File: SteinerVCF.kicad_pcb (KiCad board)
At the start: 2 copper layers, 39.6 x 100 mm, 72 parts, among them J1 AudioJack2_Ground_Switch, J2 AudioJack2_Ground_Switch, J3 AudioJack2_Ground_Switch, J4 AudioJack2_Ground_Switch, J5 AudioJack2_Ground_Switch, J6 AudioJack2_Ground_Switch, J7 Conn_02x05_Odd_Even, J8 AudioJack2_Ground_Switch, J9 AudioJack2_Ground_Switch, Q1 BC847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

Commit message: Added bourns trimmer 3-d model.
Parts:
- RV4: footprint Potentiometer_THT:Potentiometer_Bourns_3296W_Vertical -> Local:Bourns3296WV
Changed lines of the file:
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@@
-(kicad_pcb (version 20171130) (host pcbnew "(5.0.1-3-g963ef8bb5)")
+(kicad_pcb (version 20171130) (host pcbnew "(5.0.0)")
   (general
     (thickness 1.6)
@@
     (aux_axis_origin 148.5 105)
     (grid_origin 148.5 105)
-    (visible_elements FFFFFF7F)
+    (visible_elements 7FFFFFFF)
     (pcbplotparams
       (layerselection 0x010f4_ffffffff)
@@
     (add_net "Net-(R9-Pad2)")
   )
+  (module Local:Bourns3296WV (layer B.Cu)
+    (at 164.883 102.46 90)
+    (descr "Potentiometer, vertical, Bourns 3296W, https://www.bourns.com/pdfs/3296.pdf")
+    (tags "Potentiometer vertical Bourns 3296W")
+    (fp_text reference RV4 (at -2.54 -3.429 90) (layer B.SilkS)
+      (effects (font (size 0.75 1) (thickness 0.125)) (justify mirror))
+    )
+    (fp_text value 2k (at -2.54 -3.67 90) (layer B.Fab)
+      (effects (font (size 1 1) (thickness 0.15)) (justify mirror))
+    )
+    (fp_circle (center 0.955 -1.15) (end 2.05 -1.15) (layer B.Fab) (width 0.1))
+    (fp_line (start -7.305 2.41) (end -7.305 -2.42) (layer B.Fab) (width 0.1))
+    (fp_line (start -7.305 -2.42) (end 2.225 -2.42) (layer B.Fab) (width 0.1))
+    (fp_line (start 2.225 -2.42) (end 2.225 2.41) (layer B.Fab) (width 0.1))
+    (fp_line (start 2.225 2.41) (end -7.305 2.41) (layer B.Fab) (width 0.1))
+    (fp_line (start 0.955 -2.235) (end 0.956 -0.066) (layer B.Fab) (width 0.1))
+    (fp_line (start 0.955 -2.235) (end 0.956 -0.066) (layer B.Fab) (width 0.1))
+    (fp_line (start -7.425 2.53) (end 2.345 2.53) (layer B.SilkS) (width 0.12))
+    (fp_line (start -7.425 -2.54) (end 2.345 -2.54) (layer B.SilkS) (width 0.12))
+    (fp_line (start -7.425 2.53) (end -7.425 -2.54) (layer B.SilkS) (width 0.12))
+    (fp_line (start 2.345 2.53) (end 2.345 -2.54) (layer B.SilkS) (width 0.12))
+    (fp_line (start -7.6 2.7) (end -7.6 -2.7) (layer B.CrtYd) (width 0.05))
+    (fp_line (start -7.6 -2.7) (end 2.5 -2.7) (layer B.CrtYd) (width 0.05))
+    (fp_line (start 2.5 -2.7) (end 2.5 2.7) (layer B.CrtYd) (width 0.05))
+    (fp_line (start 2.5 2.7) (end -7.6 2.7) (layer B.CrtYd) (width 0.05))
+    (fp_text user %R (at -3.175 -0.005 90) (layer B.Fab)
+      (effects (font (size 1 1) (thickness 0.15)) (justify mirror))
+    )
+    (pad 1 thru_hole circle (at 0 0 90) (size 1.44 1.44) (drill 0.8) (layers *.Cu *.Mask)
+      (net 27 "Net-(R9-Pad2)"))
+    (pad 2 thru_hole circle (at -2.54 0 90) (size 1.44 1.44) (drill 0.8) (layers *.Cu *.Mask)
+      (net 27 "Net-(R9-Pad2)"))
+    (pad 3 thru_hole circle (at -5.08 0 90) (size 1.44 1.44) (drill 0.8) (layers *.Cu *.Mask)
+      (net 55 GND))
+    (model ${KISYS3DMOD}/Potentiometer_THT.3dshapes/Potentiometer_Bourns_3296W_Vertical.wrl
+      (at (xyz 0 0 0))
+      (scale (xyz 1 1 1))
+      (rotate (xyz 0 0 0))
+    )
+    (model ${KIPRJMOD}/Local.pretty/Bourns3296WV.step
+      (offset (xyz -5 0 0))
+      (scale (xyz 1 1 1))
+      (rotate (xyz 90 0 0))
+    )
+  )
   (module Local:PJ398SM (layer F.Cu)
     (at 158.66 135.48)
@@
       (at (xyz 0 0 0))
       (scale (xyz 1 1 1))
-      (rotate (xyz 0 0 0))
-    )
-  )
-  (module Potentiometer_THT:Potentiometer_Bourns_3296W_Vertical (layer B.Cu)
-    (at 164.883 102.46 90)
-    (descr "Potentiometer, vertical, Bourns 3296W, https://www.bourns.com/pdfs/3296.pdf")
-    (tags "Potentiometer vertical Bourns 3296W")
-    (fp_text reference RV4 (at -2.54 -3.429 90) (layer B.SilkS)
-      (effects (font (size 0.75 1) (thickness 0.125)) (justify mirror))
-    )
-    (fp_text value 2k (at -2.54 -3.67 90) (layer B.Fab)
-      (effects (font (size 1 1) (thickness 0.15)) (justify mirror))
-    )
-    (fp_circle (center 0.955 -1.15) (end 2.05 -1.15) (layer B.Fab) (width 0.1))
-    (fp_line (start -7.305 2.41) (end -7.305 -2.42) (layer B.Fab) (width 0.1))
-    (fp_line (start -7.305 -2.42) (end 2.225 -2.42) (layer B.Fab) (width 0.1))
-    (fp_line (start 2.225 -2.42) (end 2.225 2.41) (layer B.Fab) (width 0.1))
-    (fp_line (start 2.225 2.41) (end -7.305 2.41) (layer B.Fab) (width 0.1))
-    (fp_line (start 0.955 -2.235) (end 0.956 -0.066) (layer B.Fab) (width 0.1))
-    (fp_line (start 0.955 -2.235) (end 0.956 -0.066) (layer B.Fab) (width 0.1))
-    (fp_line (start -7.425 2.53) (end 2.345 2.53) (layer B.SilkS) (width 0.12))
-    (fp_line (start -7.425 -2.54) (end 2.345 -2.54) (layer B.SilkS) (width 0.12))
-    (fp_line (start -7.425 2.53) (end -7.425 -2.54) (layer B.SilkS) (width 0.12))
-    (fp_line (start 2.345 2.53) (end 2.345 -2.54) (layer B.SilkS) (width 0.12))
-    (fp_line (start -7.6 2.7) (end -7.6 -2.7) (layer B.CrtYd) (width 0.05))
-    (fp_line (start -7.6 -2.7) (end 2.5 -2.7) (layer B.CrtYd) (width 0.05))
-    (fp_line (start 2.5 -2.7) (end 2.5 2.7) (layer B.CrtYd) (width 0.05))
-    (fp_line (start 2.5 2.7) (end -7.6 2.7) (layer B.CrtYd) (width 0.05))
-    (fp_text user %R (at -3.175 -0.005 90) (layer B.Fab)
-      (effects (font (size 1 1) (thickness 0.15)) (justify mirror))
-    )
-    (pad 1 thru_hole circle (at 0 0 90) (size 1.44 1.44) (drill 0.8) (layers *.Cu *.Mask)
-      (net 27 "Net-(R9-Pad2)"))
-    (pad 2 thru_hole circle (at -2.54 0 90) (size 1.44 1.44) (drill 0.8) (layers *.Cu *.Mask)
-      (net 27 "Net-(R9-Pad2)"))
-    (pad 3 thru_hole circle (at -5.08 0 90) (size 1.44 1.44) (drill 0.8) (layers *.Cu *.Mask)
-      (net 55 GND))
-    (model ${KISYS3DMOD}/Potentiometer_THT.3dshapes/Potentiometer_Bourns_3296W_Vertical.wrl
-      (at (xyz 0 0 0))
-      (scale (xyz 1 1 1))

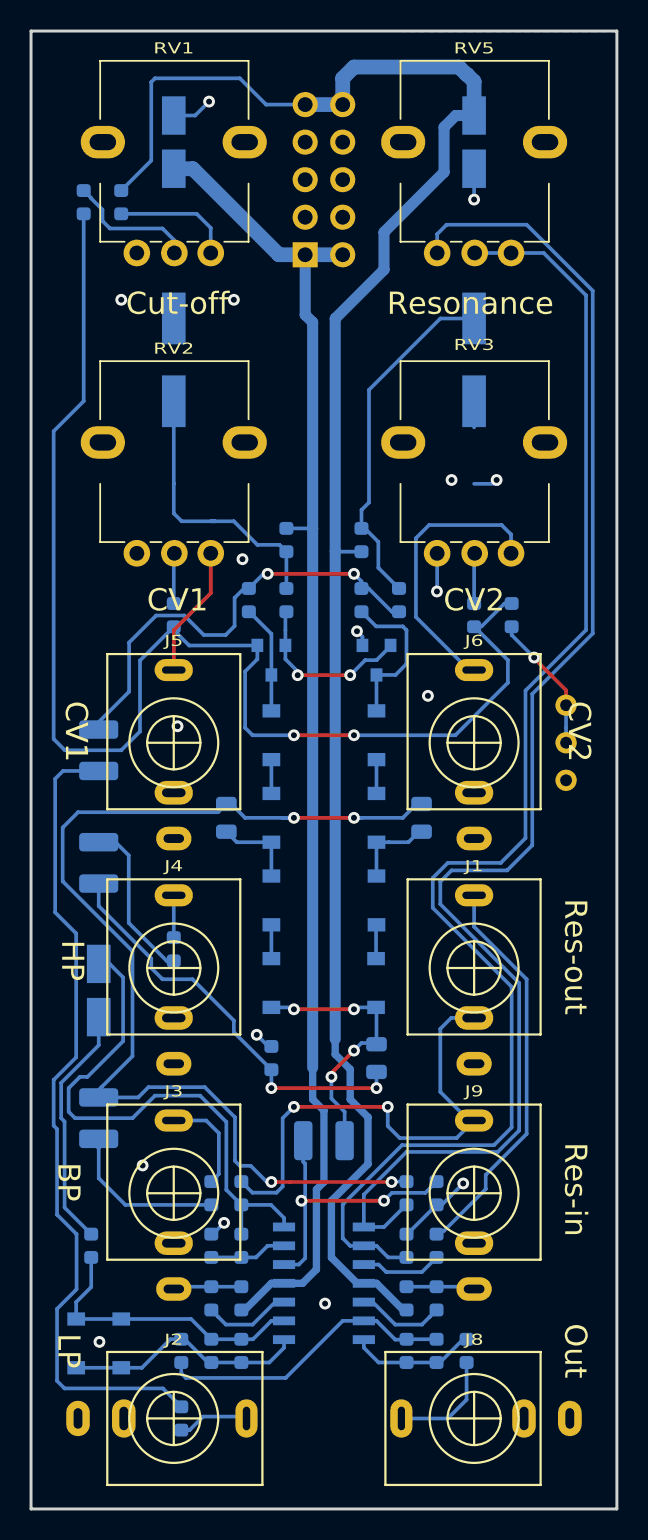
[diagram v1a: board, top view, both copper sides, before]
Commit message: Freerouted signals.
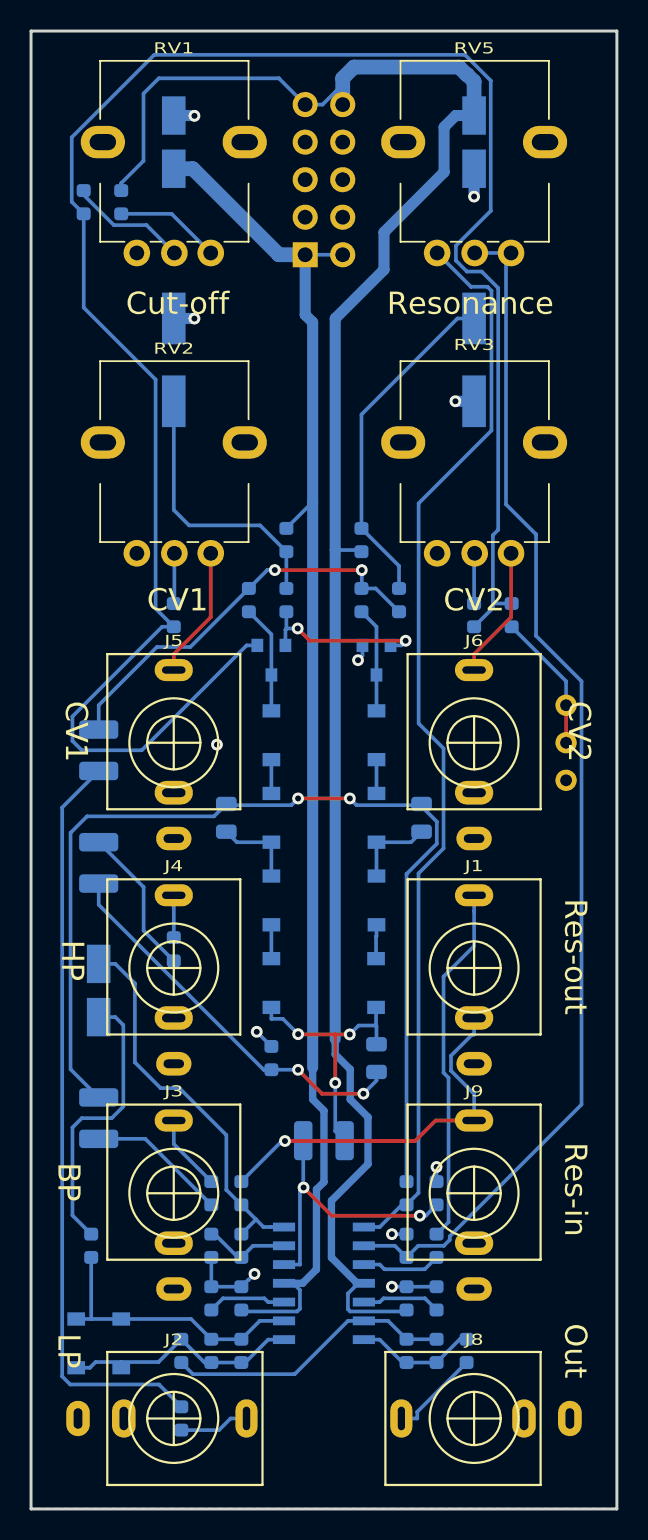
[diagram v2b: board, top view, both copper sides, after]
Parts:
- turned R16 to 90 degrees
- turned R18 to 270 degrees
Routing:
- net Net-(Q1-Pad1): track 90.7 -> 135.7 mm, vias 2 -> 0
- net Net-(R17-Pad1): track 97.4 -> 73.9 mm
- net /Resonance: track 94.9 -> 81.8 mm
- net Net-(C12-Pad1): track 37.6 -> 26.6 mm
- net GND: track 29.3 -> 19.0 mm, vias 17 -> 11
- net /CV2: track 19.1 -> 8.94 mm
- net LoopOut: track 34.7 -> 25.8 mm, vias 2 -> 1
- net Net-(C1-Pad2): track 55.5 -> 50.9 mm
- net Net-(D8-Pad2): track 10.6 -> 7.13 mm
- net Net-(C1-Pad1): track 30.9 -> 27.7 mm
- net Net-(C2-Pad1): track 73.6 -> 70.5 mm, vias 4 -> 2
- net -12V: track 91.2 -> 94.3 mm
- net LoopIn: track 27.1 -> 24.3 mm
- net +12V: track 127.8 -> 130.6 mm
- net Net-(C12-Pad2): track 16.6 -> 19.2 mm
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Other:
- board text added: "Rev B"
- board text removed: "Rev A"
